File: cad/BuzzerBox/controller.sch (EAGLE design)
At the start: 126 parts, among them J1 USB_A_SMT_FEMALE, Q1 BSS138, Q2 BSS138, Q3 BSS138, T1 BC849, T10 BC849, T2 BC849, T3 BC849, T4 BC849, T5 BC849, T6 BC849, T7 BC849, T8 BC849, T9 BC849, U1 ATMEGA328P-AU, Y1 16MHz

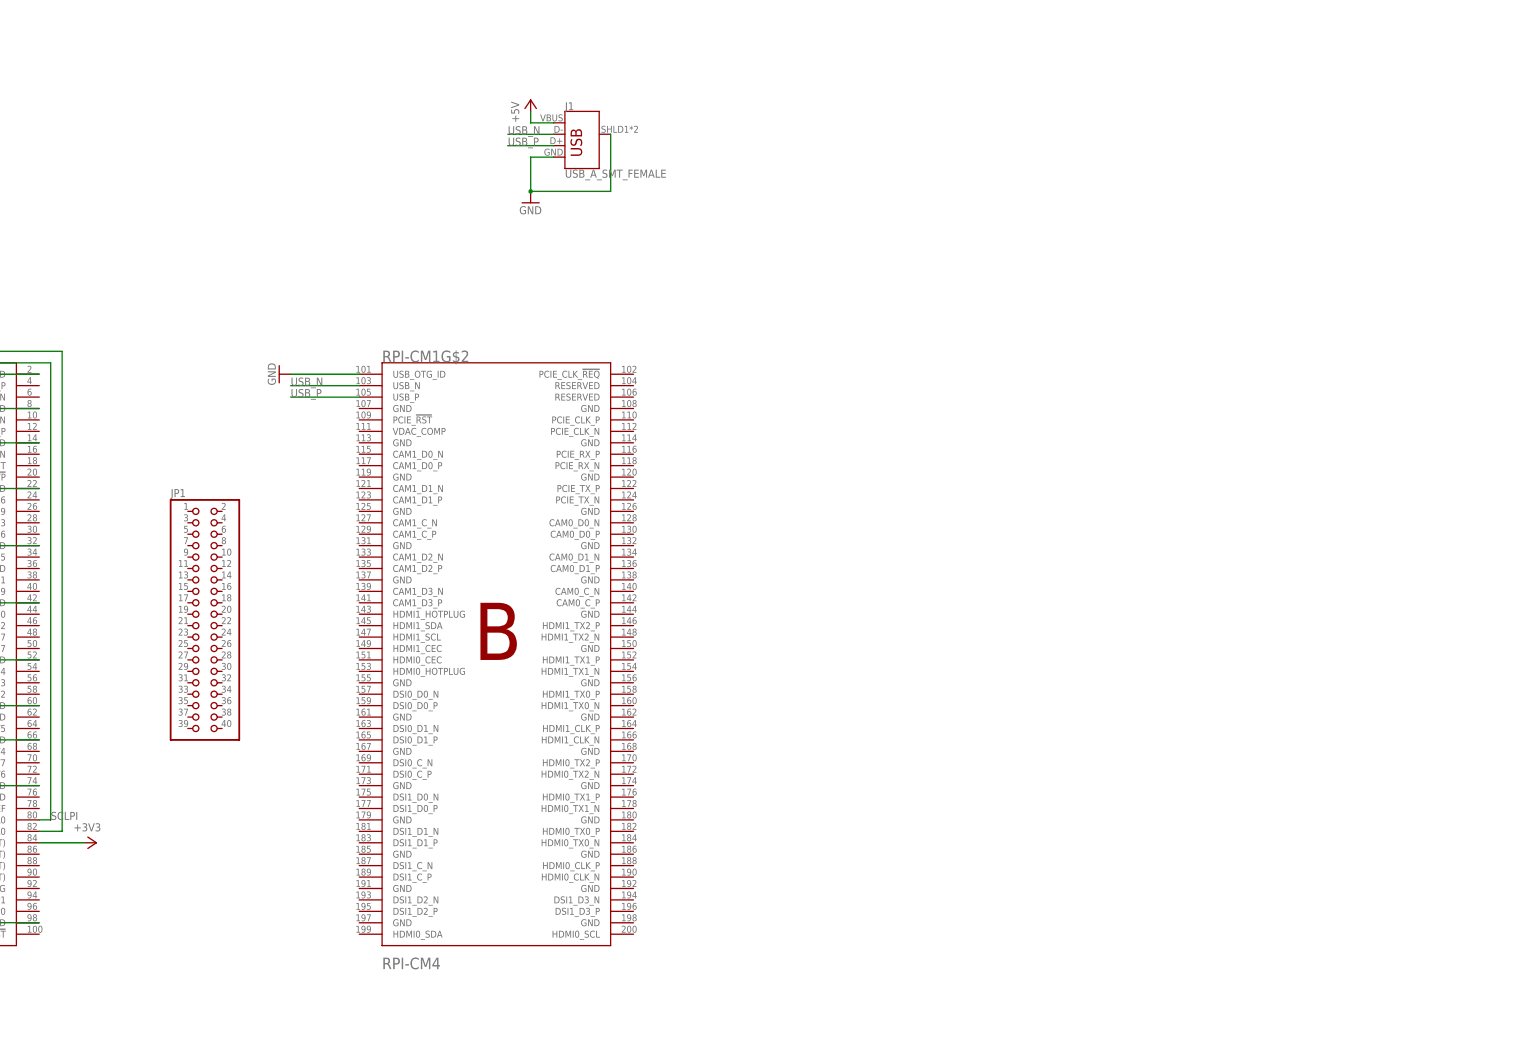
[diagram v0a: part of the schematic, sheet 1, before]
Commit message: Added HDMI
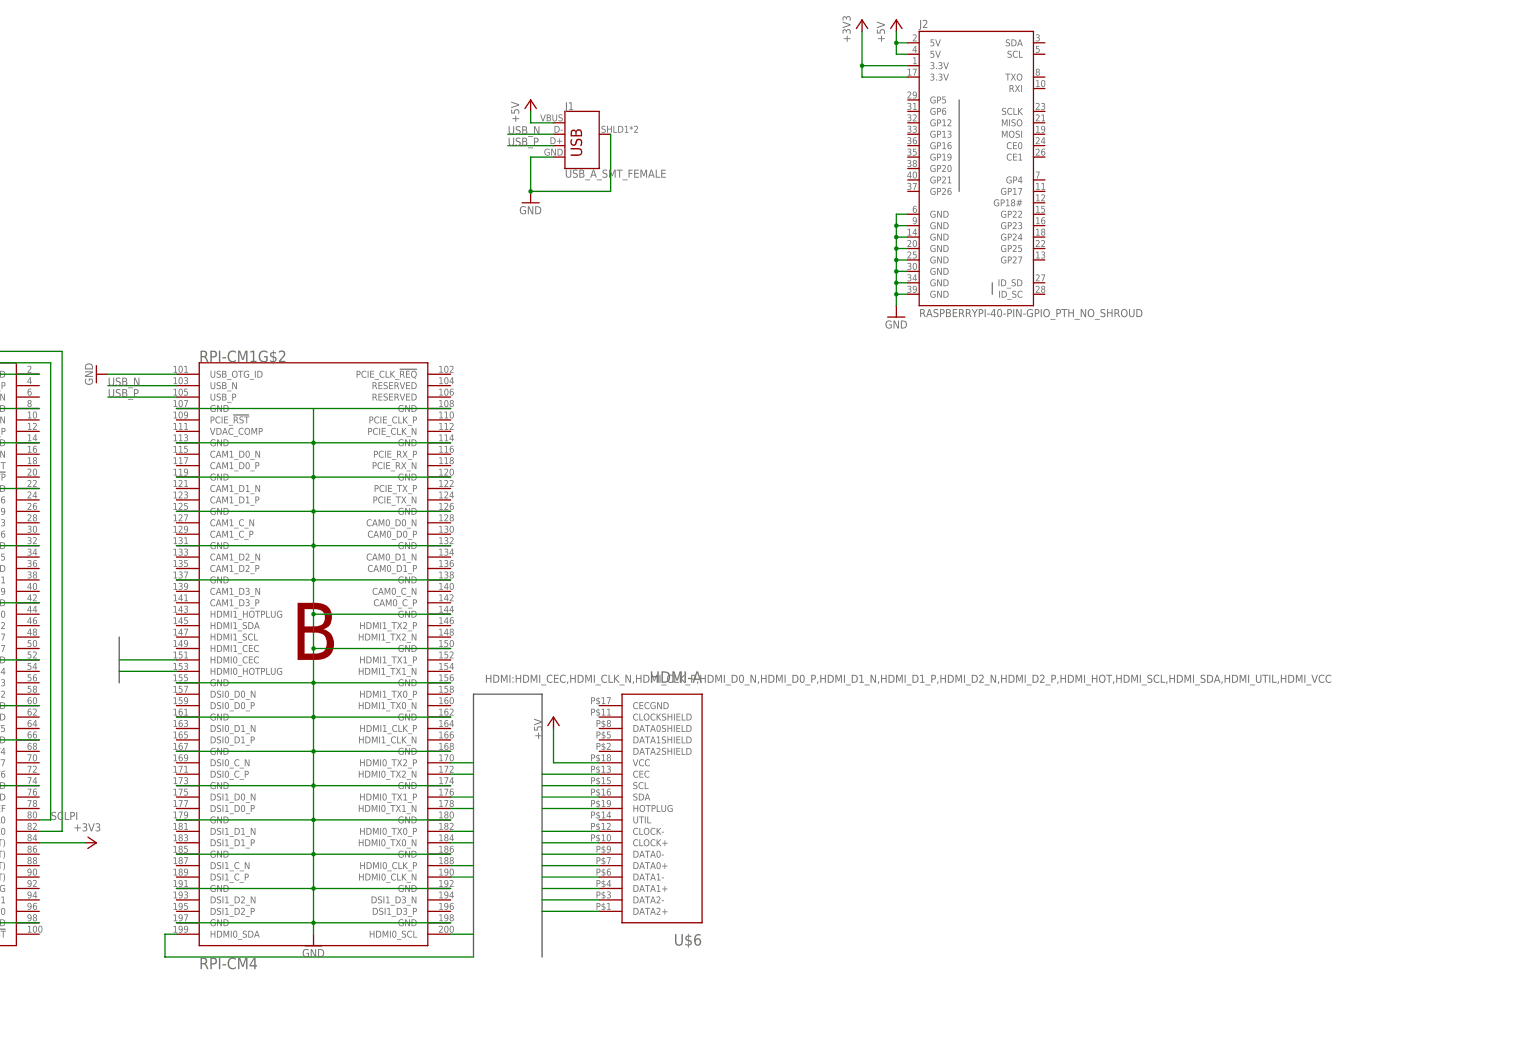
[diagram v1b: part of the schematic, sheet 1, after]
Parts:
- removed JP1: (no value), pinhead:PINHD-2X20
- added J2: RASPBERRYPI-40-PIN-GPIO_PTH_NO_SHROUD, Custom-Connector:RASPBERRYPI-40-PIN-GPIO_PTH_NO_SHROUD
- added U$6: HDMI-A, connectors:HDMI-A
- J1: device SparkFun-Connectors:USB_A_SMT_FEMALE -> Custom-Connector:USB_A_SMT_FEMALE
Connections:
- new net HDMI_CEC: RPI-CM1G$2.HDMI0_CEC, U$6.CEC
- new net HDMI_CLK_N: RPI-CM1G$2.HDMI0_CLK_N, U$6.CLOCK-
- new net HDMI_CLK_P: RPI-CM1G$2.HDMI0_CLK_P, U$6.CLOCK+
- new net HDMI_D0_N: RPI-CM1G$2.HDMI0_TX0_N, U$6.DATA0-
- new net HDMI_D0_P: RPI-CM1G$2.HDMI0_TX0_P, U$6.DATA0+
- new net HDMI_D1_N: RPI-CM1G$2.HDMI0_TX1_N, U$6.DATA1-
- new net HDMI_D1_P: RPI-CM1G$2.HDMI0_TX1_P, U$6.DATA1+
- new net HDMI_D2_N: RPI-CM1G$2.HDMI0_TX2_N, U$6.DATA2-
- new net HDMI_D2_P: RPI-CM1G$2.HDMI0_TX2_P, U$6.DATA2+
- new net HDMI_HOT: RPI-CM1G$2.HDMI0_HOTPLUG, U$6.HOTPLUG
- new net HDMI_SCL: RPI-CM1G$2.HDMI0_SCL, U$6.SCL
- new net HDMI_SDA: RPI-CM1G$2.HDMI0_SDA, U$6.SDA
- net +3V3: now also J2.3.3V@1, J2.3.3V@17
- net +5V: now also J2.5V@2, J2.5V@4, U$6.VCC
- net GND: now also J2.GND@14, J2.GND@20, J2.GND@25, J2.GND@30, J2.GND@34, J2.GND@39, J2.GND@6, J2.GND@9, RPI-CM1G$2.GND@107, RPI-CM1G$2.GND@108, RPI-CM1G$2.GND@113, RPI-CM1G$2.GND@114, RPI-CM1G$2.GND@119, RPI-CM1G$2.GND@120, RPI-CM1G$2.GND@125, RPI-CM1G$2.GND@126, RPI-CM1G$2.GND@131, RPI-CM1G$2.GND@132, RPI-CM1G$2.GND@137, RPI-CM1G$2.GND@138, RPI-CM1G$2.GND@144, RPI-CM1G$2.GND@150, RPI-CM1G$2.GND@155, RPI-CM1G$2.GND@156, RPI-CM1G$2.GND@161, RPI-CM1G$2.GND@162, RPI-CM1G$2.GND@167, RPI-CM1G$2.GND@168, RPI-CM1G$2.GND@173, RPI-CM1G$2.GND@174, RPI-CM1G$2.GND@179, RPI-CM1G$2.GND@180, RPI-CM1G$2.GND@185, RPI-CM1G$2.GND@186, RPI-CM1G$2.GND@191, RPI-CM1G$2.GND@192, RPI-CM1G$2.GND@197, RPI-CM1G$2.GND@198
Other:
- moved on the sheet: RPI-CM1G$2

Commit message: Add pin header to support external PI
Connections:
- removed net N$41: Q1.S, R32.1, RPI-CM1G$1.SDA0
- removed net N$47: Q3.S, R67.1, RPI-CM1G$1.GPIO14
- new net GP10: J2.MOSI, RPI-CM1G$1.GPIO10
- new net GP11: J2.SCLK, RPI-CM1G$1.GPIO11
- new net GP12: J2.GP12, RPI-CM1G$1.GPIO12
- new net GP13: J2.GP13, RPI-CM1G$1.GPIO13
- new net GP14: J2.TXO, RPI-CM1G$1.GPIO14
- new net GP15: J2.RXI, RPI-CM1G$1.GPIO15
- new net GP16: J2.GP16, RPI-CM1G$1.GPIO16
- new net GP17: J2.GP17, RPI-CM1G$1.GPIO17
- new net GP18: J2.GP18#, RPI-CM1G$1.GPIO18
- new net GP19: J2.GP19, RPI-CM1G$1.GPIO19
- new net GP2: RPI-CM1G$1.GPIO2
- new net GP20: J2.GP20, RPI-CM1G$1.GPIO20
- new net GP21: J2.GP21, RPI-CM1G$1.GPIO21
- new net GP22: J2.GP22, RPI-CM1G$1.GPIO22
- new net GP23: J2.GP23, Q3.S, R67.1, RPI-CM1G$1.GPIO23
- new net GP24: J2.GP24, RPI-CM1G$1.GPIO24
- new net GP25: J2.GP25, RPI-CM1G$1.GPIO25
- new net GP26: J2.GP26, RPI-CM1G$1.GPIO26
- new net GP27: J2.GP27, RPI-CM1G$1.GPIO27
- new net GP3: RPI-CM1G$1.GPIO3
- new net GP4: J2.GP4, RPI-CM1G$1.GPIO4
- new net GP5: J2.GP5, RPI-CM1G$1.GPIO5
- new net GP6: J2.GP6, RPI-CM1G$1.GPIO6
- new net GP7: J2.CE1, RPI-CM1G$1.GPIO7
- new net GP8: J2.CE0, RPI-CM1G$1.GPIO8
- new net GP9: J2.MISO, RPI-CM1G$1.GPIO9
- new net ID_SC: J2.ID_SC, RPI-CM1G$1.ID_SC
- new net ID_SD: J2.ID_SD, RPI-CM1G$1.ID_SD
- new net SDAPI: J2.SDA, Q1.S, R32.1, RPI-CM1G$1.SDA0
- net GND: now also U$6.CECGND, U$6.CLOCKSHIELD, U$6.DATA0SHIELD, U$6.DATA1SHIELD, U$6.DATA2SHIELD
- net SCLPI: now also J2.SCL

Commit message: Organize Sikscreen
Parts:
- renumbered J1 to USB0, MCP23017 to MCP2, RPI-CM1 to RPI-CM4, U$6 to HDMI0

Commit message: Length match differential paris
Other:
- moved on the sheet: HDMI0, J2, RPI-CM4G$1, RPI-CM4G$2, USB0

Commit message: Connect necessary CM4 pins, according to documentation
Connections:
- net +3V3: now also RPI-CM4G$1.CM4_3.3V(OUTPUT)@86, RPI-CM4G$1.GPIO_VREF
- net GND: now also RPI-CM4G$1.EEPROM_!WP
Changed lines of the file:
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@@
 <part name="GND44" library="supply1" library_urn="urn:adsk.eagle:library:371" deviceset="GND" device=""/>
 <part name="FRAME3" library="frames" library_urn="urn:adsk.eagle:library:229" deviceset="A3L-LOC" device=""/>
+<part name="GND45" library="supply1" library_urn="urn:adsk.eagle:library:371" deviceset="GND" device=""/>
 </parts>
 <sheets>
@@
 <instance part="GND44" gate="1" x="195.58" y="73.66" smashed="yes">
 <attribute name="VALUE" x="193.04" y="71.12" size="1.778" layer="96"/>
+</instance>
+<instance part="GND45" gate="1" x="88.9" y="132.08" smashed="yes" rot="R90">
+<attribute name="VALUE" x="91.44" y="129.54" size="1.778" layer="96" rot="R90"/>
 </instance>
 </instances>
@@
 <wire x1="195.58" y1="81.28" x2="198.12" y2="81.28" width="0.1524" layer="91"/>
 </segment>
+<segment>
+<pinref part="RPI-CM4" gate="G$1" pin="EEPROM_!WP"/>
+<pinref part="GND45" gate="1" pin="GND"/>
+<wire x1="76.2" y1="132.08" x2="86.36" y2="132.08" width="0.1524" layer="91"/>
+</segment>
 </net>
 <net name="+3V3" class="0">
@@
 <pinref part="RPI-CM4" gate="G$1" pin="CM4_3.3V(OUTPUT)@84"/>
 <pinref part="+3V2" gate="G$1" pin="+3V3"/>
-<wire x1="76.2" y1="50.8" x2="86.36" y2="50.8" width="0.1524" layer="91"/>
-</segment>
-<segment>
+<wire x1="76.2" y1="50.8" x2="83.82" y2="50.8" width="0.1524" layer="91"/>
+<pinref part="RPI-CM4" gate="G$1" pin="CM4_3.3V(OUTPUT)@86"/>
+<wire x1="83.82" y1="50.8" x2="86.36" y2="50.8" width="0.1524" layer="91"/>
+<wire x1="76.2" y1="48.26" x2="83.82" y2="48.26" width="0.1524" layer="91"/>
+<wire x1="83.82" y1="48.26" x2="83.82" y2="50.8" width="0.1524" layer="91"/>
+<junction x="83.82" y="50.8"/>
+<pinref part="RPI-CM4" gate="G$1" pin="GPIO_VREF"/>
+<wire x1="76.2" y1="58.42" x2="83.82" y2="58.42" width="0.1524" layer="91"/>
+<wire x1="83.82" y1="58.42" x2="83.82" y2="50.8" width="0.1524" layer="91"/>
+</segment>
+<segment>

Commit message: Ground HDMI chassis, add overvoltage protection
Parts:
- added D1: (no value), diode:ZENER-DIODESMB
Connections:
- net +5V: now also D1.C
- net GND: now also D1.A, HDMI0.SHIELD
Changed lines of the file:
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@@
 <part name="FRAME3" library="frames" library_urn="urn:adsk.eagle:library:229" deviceset="A3L-LOC" device=""/>
 <part name="GND45" library="supply1" library_urn="urn:adsk.eagle:library:371" deviceset="GND" device=""/>
+<part name="D1" library="diode" library_urn="urn:adsk.eagle:library:210" deviceset="ZENER-DIODE" device="SMB" package3d_urn="urn:adsk.eagle:package:43404/2"/>
 </parts>
 <sheets>
@@
 <wire x1="195.58" y1="76.2" x2="195.58" y2="81.28" width="0.1524" layer="91"/>
 <wire x1="195.58" y1="81.28" x2="198.12" y2="81.28" width="0.1524" layer="91"/>
+<pinref part="HDMI0" gate="G$1" pin="SHIELD"/>
+<wire x1="200.66" y1="83.82" x2="195.58" y2="83.82" width="0.1524" layer="91"/>
+<wire x1="195.58" y1="83.82" x2="195.58" y2="81.28" width="0.1524" layer="91"/>
+<junction x="195.58" y="81.28"/>
 </segment>
 <segment>
@@
 <attribute name="VALUE" x="226.06" y="177.8" size="1.778" layer="96"/>
 </instance>
+<instance part="D1" gate="G$1" x="185.42" y="191.516" smashed="yes" rot="R90">
+<attribute name="NAME" x="183.515" y="189.738" size="1.778" layer="95" rot="R90"/>
+<attribute name="VALUE" x="188.849" y="189.738" size="1.778" layer="96" rot="R90"/>
+</instance>
 </instances>
 <busses>
@@
 <pinref part="POWER" gate="-1" pin="K"/>
 <wire x1="172.72" y1="187.96" x2="172.72" y2="182.88" width="0.1524" layer="91"/>
+<pinref part="D1" gate="G$1" pin="A"/>
+<junction x="172.72" y="187.96"/>
+<wire x1="172.72" y1="187.96" x2="185.42" y2="187.96" width="0.1524" layer="91"/>
+<wire x1="185.42" y1="187.96" x2="185.42" y2="188.976" width="0.1524" layer="91"/>
 </segment>
 <segment>
@@
 <pinref part="D3" gate="1" pin="C"/>
 <wire x1="181.356" y1="195.628" x2="181.356" y2="195.58" width="0.1524" layer="91"/>
-</segment>
-<segment>
+<pinref part="D1" gate="G$1" pin="C"/>
+<wire x1="185.42" y1="194.056" x2="185.42" y2="195.58" width="0.1524" layer="91"/>
+<junction x="185.42" y="195.58"/>
+</segment>
+<segment>

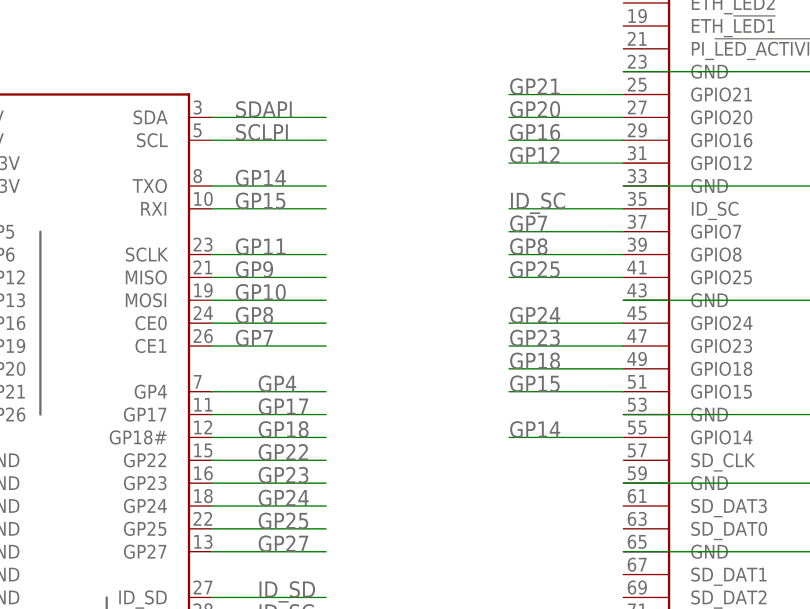
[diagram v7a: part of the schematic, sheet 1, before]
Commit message: Changed to 4 layer stackup
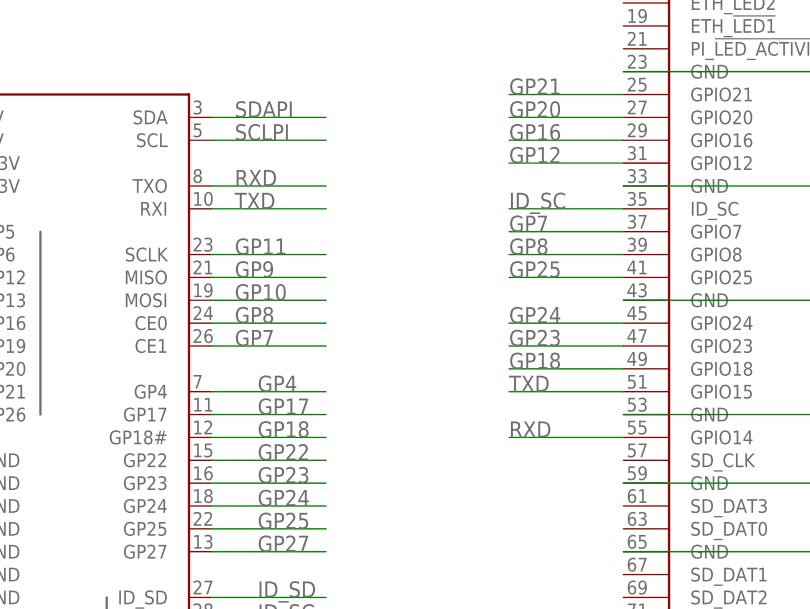
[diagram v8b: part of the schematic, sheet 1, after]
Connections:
- removed net GP14: J2.TXO, RPI-CM4G$1.GPIO14
- removed net GP15: J2.RXI, RPI-CM4G$1.GPIO15
- removed net N$48: U1.PD1
- removed net N$49: U1.PD0
- new net RXD: J2.TXO, RPI-CM4G$1.GPIO14, U1.PD0
- new net TXD: J2.RXI, RPI-CM4G$1.GPIO15, U1.PD1
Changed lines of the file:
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@@
 <class number="0" name="default" width="0" drill="0">
 </class>
+<class number="1" name="USB" width="0.17500625" drill="0">
+</class>
 </classes>
 <parts>
@@
 </segment>
 </net>
-<net name="USB_N" class="0">
+<net name="USB_N" class="1">
 <segment>
 <pinref part="RPI-CM4" gate="G$2" pin="USB_N"/>
@@
 </segment>
 </net>
-<net name="USB_P" class="0">
+<net name="USB_P" class="1">
 <segment>
 <pinref part="RPI-CM4" gate="G$2" pin="USB_P"/>
@@
 </segment>
 </net>
-<net name="GP15" class="0">
-<segment>
-<pinref part="RPI-CM4" gate="G$1" pin="GPIO15"/>
-<wire x1="15.24" y1="91.44" x2="2.54" y2="91.44" width="0.1524" layer="91"/>
-<label x="2.54" y="91.44" size="1.778" layer="95"/>
-</segment>
-<segment>
-<pinref part="J2" gate="G$1" pin="RXI"/>
-<wire x1="-30.48" y1="111.76" x2="-17.78" y2="111.76" width="0.1524" layer="91"/>
-<label x="-27.94" y="111.76" size="1.778" layer="95"/>
-</segment>
-</net>
-<net name="GP14" class="0">
-<segment>
-<pinref part="RPI-CM4" gate="G$1" pin="GPIO14"/>
-<wire x1="15.24" y1="86.36" x2="2.54" y2="86.36" width="0.1524" layer="91"/>
-<label x="2.54" y="86.36" size="1.778" layer="95"/>
-</segment>
-<segment>
-<pinref part="J2" gate="G$1" pin="TXO"/>
-<wire x1="-30.48" y1="114.3" x2="-17.78" y2="114.3" width="0.1524" layer="91"/>
-<label x="-27.94" y="114.3" size="1.778" layer="95"/>
-</segment>
-</net>
 <net name="GP11" class="0">
 <segment>
@@
 </segment>
 </net>
+<net name="RXD" class="0">
+<segment>
+<pinref part="RPI-CM4" gate="G$1" pin="GPIO14"/>
+<wire x1="15.24" y1="86.36" x2="2.54" y2="86.36" width="0.1524" layer="91"/>
+<label x="2.54" y="86.36" size="1.778" layer="95"/>
+</segment>
+<segment>
+<pinref part="J2" gate="G$1" pin="TXO"/>
+<wire x1="-30.48" y1="114.3" x2="-17.78" y2="114.3" width="0.1524" layer="91"/>
+<label x="-27.94" y="114.3" size="1.778" layer="95"/>
+</segment>
+</net>
+<net name="TXD" class="0">
+<segment>
+<pinref part="RPI-CM4" gate="G$1" pin="GPIO15"/>
+<wire x1="15.24" y1="91.44" x2="2.54" y2="91.44" width="0.1524" layer="91"/>
+<label x="2.54" y="91.44" size="1.778" layer="95"/>
+</segment>
+<segment>
+<pinref part="J2" gate="G$1" pin="RXI"/>
+<wire x1="-30.48" y1="111.76" x2="-17.78" y2="111.76" width="0.1524" layer="91"/>
+<label x="-27.94" y="111.76" size="1.778" layer="95"/>
+</segment>
+</net>
 </nets>
 </sheet>
@@
 </segment>
 </net>
-<net name="N$48" class="0">
+<net name="TXD" class="0">
 <segment>
 <pinref part="U1" gate="A" pin="PD1"/>
 <wire x1="213.36" y1="91.44" x2="226.06" y2="91.44" width="0.1524" layer="91"/>
+<label x="215.9" y="91.44" size="1.778" layer="95"/>
 </segment>
 </net>
-<net name="N$49" class="0">
+<net name="RXD" class="0">
 <segment>
 <pinref part="U1" gate="A" pin="PD0"/>
 <wire x1="213.36" y1="93.98" x2="226.06" y2="93.98" width="0.1524" layer="91"/>
+<label x="215.9" y="93.98" size="1.778" layer="95"/>
 </segment>
 </net>
